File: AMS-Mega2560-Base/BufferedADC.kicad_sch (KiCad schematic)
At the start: 5 parts, among them IC6 OPA4340UA

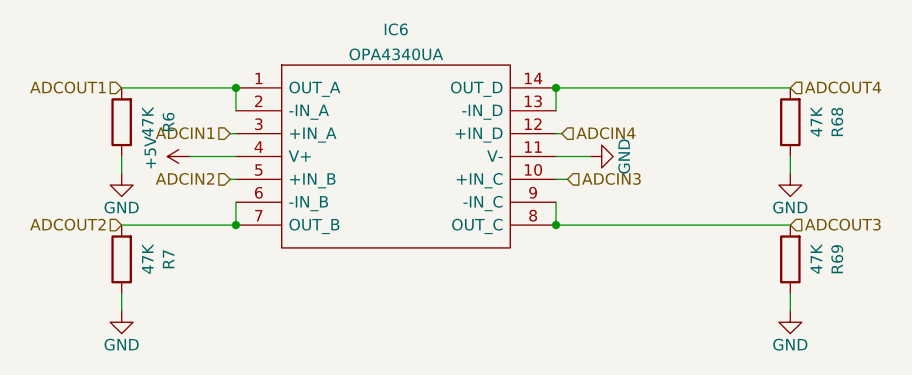
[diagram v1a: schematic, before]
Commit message: updated a few things for the SPI lines to the RTDs ready for routing.
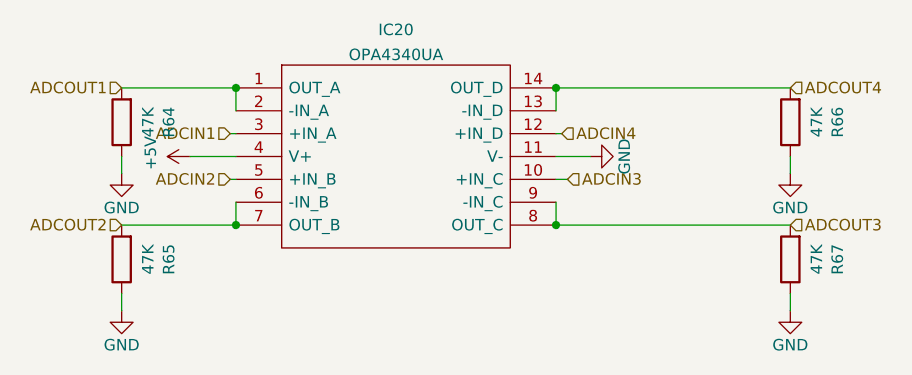
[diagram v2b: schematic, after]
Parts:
- renumbered IC6 to IC20, R6 to R64, R7 to R65, R68 to R66, R69 to R67
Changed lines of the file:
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@@
   (symbol (lib_id "Device:R") (at 118.745 62.865 180)
     (in_bom yes) (on_board yes)
-    (property "Reference" "R6" (id 0) (at 124.0028 62.865 90))
+    (property "Reference" "R64" (id 0) (at 124.0028 62.865 90))
     (property "Value" "47K" (id 1) (at 121.6914 62.865 90))
     (property "Footprint" "Resistor_THT:R_Axial_DIN0207_L6.3mm_D2.5mm_P2.54mm_Vertical" (id 2) (at 120.523 62.865 90)
@@
   (symbol (lib_id "Samac_Sys:OPA4340UA") (at 131.445 59.055 0)
     (in_bom yes) (on_board yes) (fields_autoplaced)
-    (property "Reference" "IC6" (id 0) (at 149.225 52.5993 0))
+    (property "Reference" "IC20" (id 0) (at 149.225 52.5993 0))
     (property "Value" "OPA4340UA" (id 1) (at 149.225 55.3744 0))
     (property "Footprint" "SOIC127P600X175-14N" (id 2) (at 163.195 56.515 0)
@@
   (symbol (lib_id "power:GND") (at 170.815 66.675 90)
     (in_bom yes) (on_board yes)
-    (property "Reference" "#PWR0143" (id 0) (at 177.165 66.675 0)
+    (property "Reference" "#PWR085" (id 0) (at 177.165 66.675 0)
       (effects (font (size 1.27 1.27)) hide)
     )
@@
   (symbol (lib_id "Device:R") (at 118.745 78.105 180)
     (in_bom yes) (on_board yes)
-    (property "Reference" "R7" (id 0) (at 124.0028 78.105 90))
+    (property "Reference" "R65" (id 0) (at 124.0028 78.105 90))
     (property "Value" "47K" (id 1) (at 121.6914 78.105 90))
     (property "Footprint" "Resistor_THT:R_Axial_DIN0207_L6.3mm_D2.5mm_P2.54mm_Vertical" (id 2) (at 120.523 78.105 90)
@@
   (symbol (lib_id "power:GND") (at 118.745 68.58 0)
     (in_bom yes) (on_board yes)
-    (property "Reference" "#PWR0144" (id 0) (at 118.745 74.93 0)
+    (property "Reference" "#PWR05" (id 0) (at 118.745 74.93 0)
       (effects (font (size 1.27 1.27)) hide)
     )
@@
   (symbol (lib_id "power:+5V") (at 126.365 66.675 90)
     (in_bom yes) (on_board yes)
-    (property "Reference" "#PWR0142" (id 0) (at 130.175 66.675 0)
+    (property "Reference" "#PWR082" (id 0) (at 130.175 66.675 0)
       (effects (font (size 1.27 1.27)) hide)
     )
@@
   (symbol (lib_id "Device:R") (at 193.04 62.865 180)
     (in_bom yes) (on_board yes)
-    (property "Reference" "R68" (id 0) (at 198.2978 62.865 90))
+    (property "Reference" "R66" (id 0) (at 198.2978 62.865 90))
     (property "Value" "47K" (id 1) (at 195.9864 62.865 90))
     (property "Footprint" "Resistor_THT:R_Axial_DIN0207_L6.3mm_D2.5mm_P2.54mm_Vertical" (id 2) (at 194.818 62.865 90)
@@
   (symbol (lib_id "power:GND") (at 118.745 83.82 0)
     (in_bom yes) (on_board yes)
-    (property "Reference" "#PWR0141" (id 0) (at 118.745 90.17 0)
+    (property "Reference" "#PWR067" (id 0) (at 118.745 90.17 0)
       (effects (font (size 1.27 1.27)) hide)
     )
@@
   (symbol (lib_id "power:GND") (at 193.04 68.58 0)
     (in_bom yes) (on_board yes)
-    (property "Reference" "#PWR0127" (id 0) (at 193.04 74.93 0)
+    (property "Reference" "#PWR098" (id 0) (at 193.04 74.93 0)
       (effects (font (size 1.27 1.27)) hide)
     )
@@
   (symbol (lib_id "power:GND") (at 193.04 83.82 0)
     (in_bom yes) (on_board yes)
-    (property "Reference" "#PWR0140" (id 0) (at 193.04 90.17 0)
+    (property "Reference" "#PWR0104" (id 0) (at 193.04 90.17 0)
       (effects (font (size 1.27 1.27)) hide)
     )
@@
   (symbol (lib_id "Device:R") (at 193.04 78.105 180)
     (in_bom yes) (on_board yes)
-    (property "Reference" "R69" (id 0) (at 198.2978 78.105 90))
+    (property "Reference" "R67" (id 0) (at 198.2978 78.105 90))
     (property "Value" "47K" (id 1) (at 195.9864 78.105 90))
     (property "Footprint" "Resistor_THT:R_Axial_DIN0207_L6.3mm_D2.5mm_P2.54mm_Vertical" (id 2) (at 194.818 78.105 90)
